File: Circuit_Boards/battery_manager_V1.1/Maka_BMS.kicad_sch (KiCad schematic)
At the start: 95 parts, among them J8 ‎SAM16035-ND‎, J9 Molex 087340-1424, Q1 FDC645N, Q2 FDC645N, Q3 FDC645N, Q4 Si3483CDV, Q5 Si3483CDV, Q6 FDC645N, U1 AP63205, U2 TPS70933DBV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

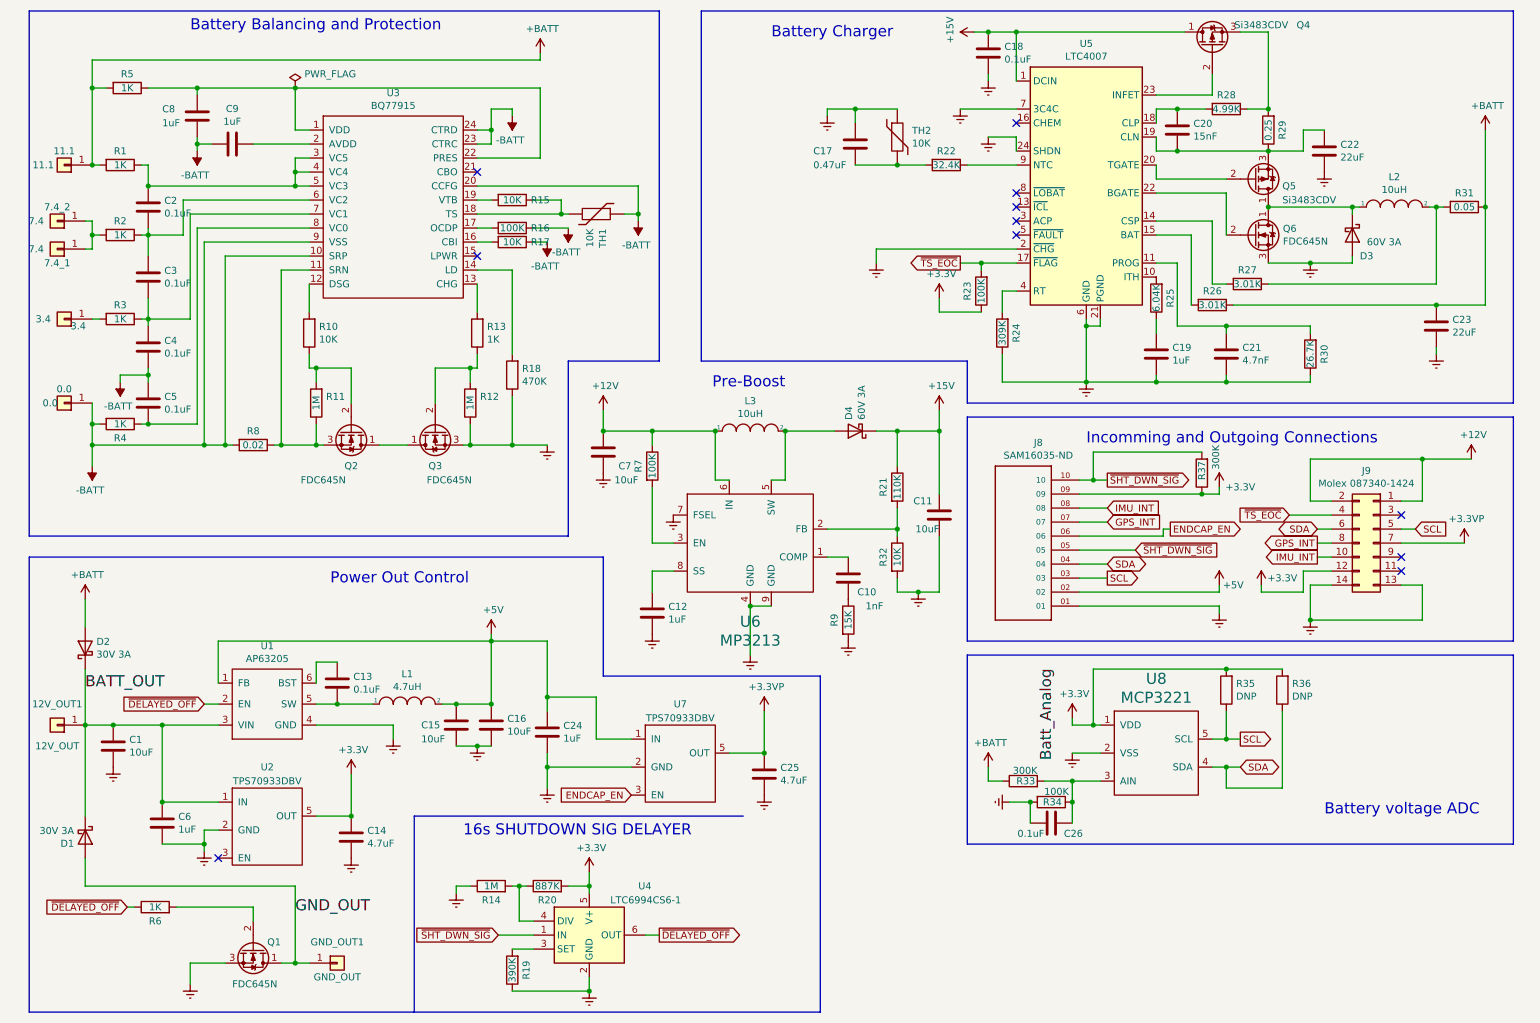
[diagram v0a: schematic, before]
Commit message: corrected part number for 10 pin BMS connector
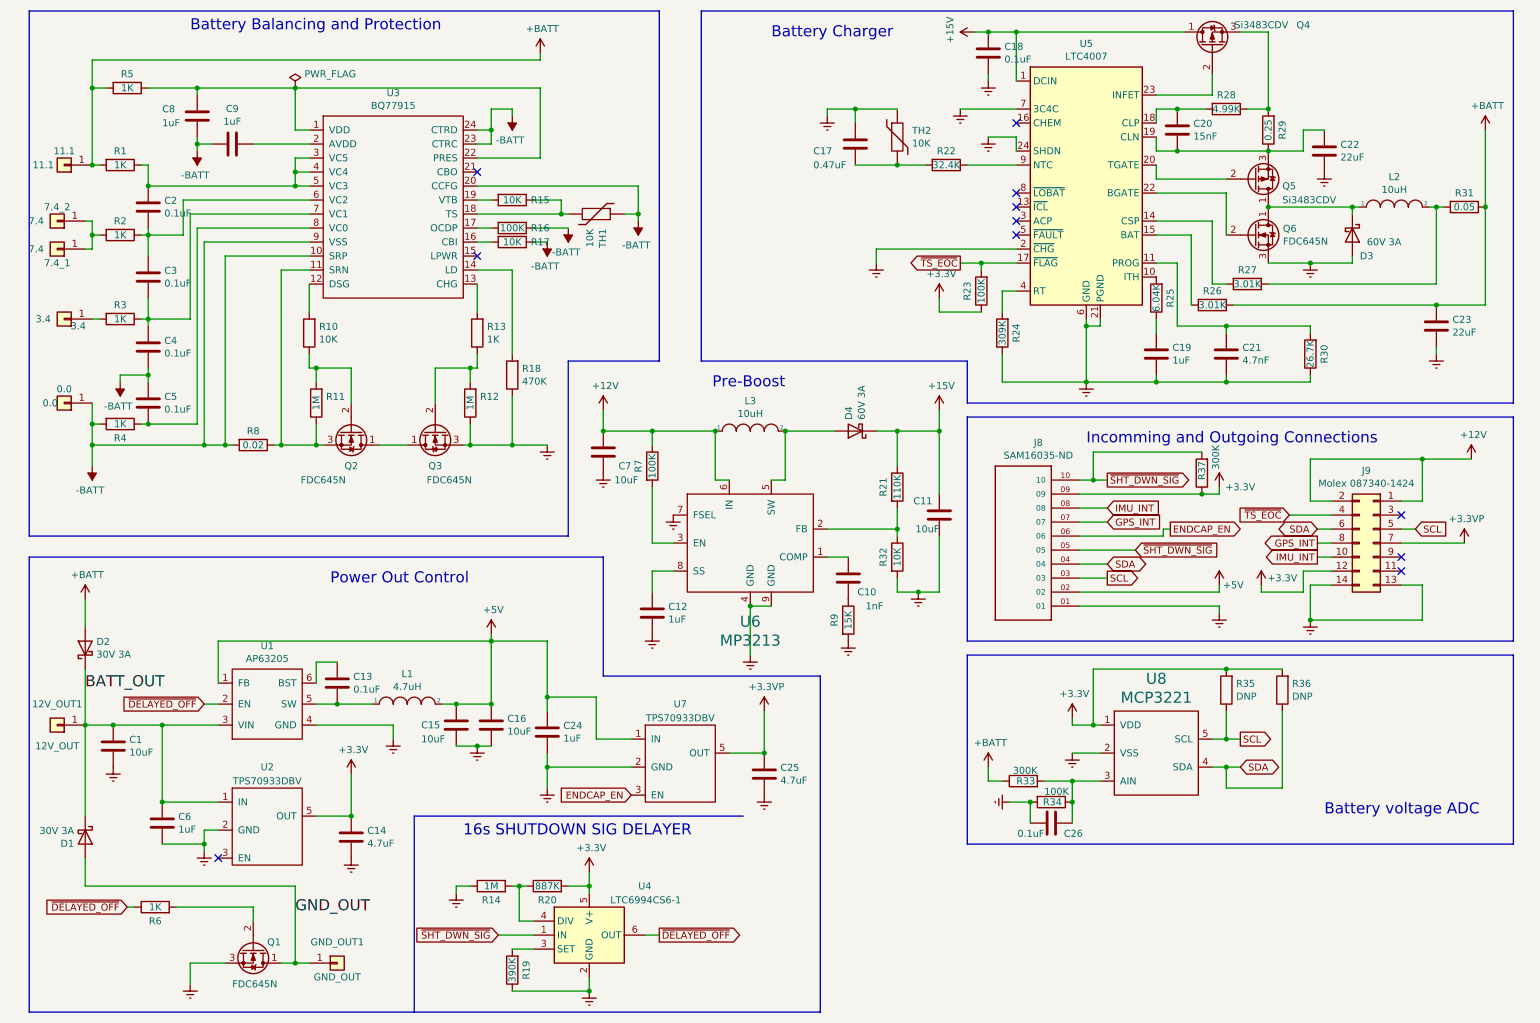
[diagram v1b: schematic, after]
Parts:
- J8: Digikey SAM11993-ND -> ‎SAM16035-ND‎
